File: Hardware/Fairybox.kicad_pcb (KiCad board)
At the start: 2 copper layers, 91.4 x 55.9 mm, 70 parts, among them J1 REED, Q1 locked, Q10 locked, Q2 locked, Q3 locked, Q4 locked, Q5 locked, Q6 locked, Q7 locked, Q8 locked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

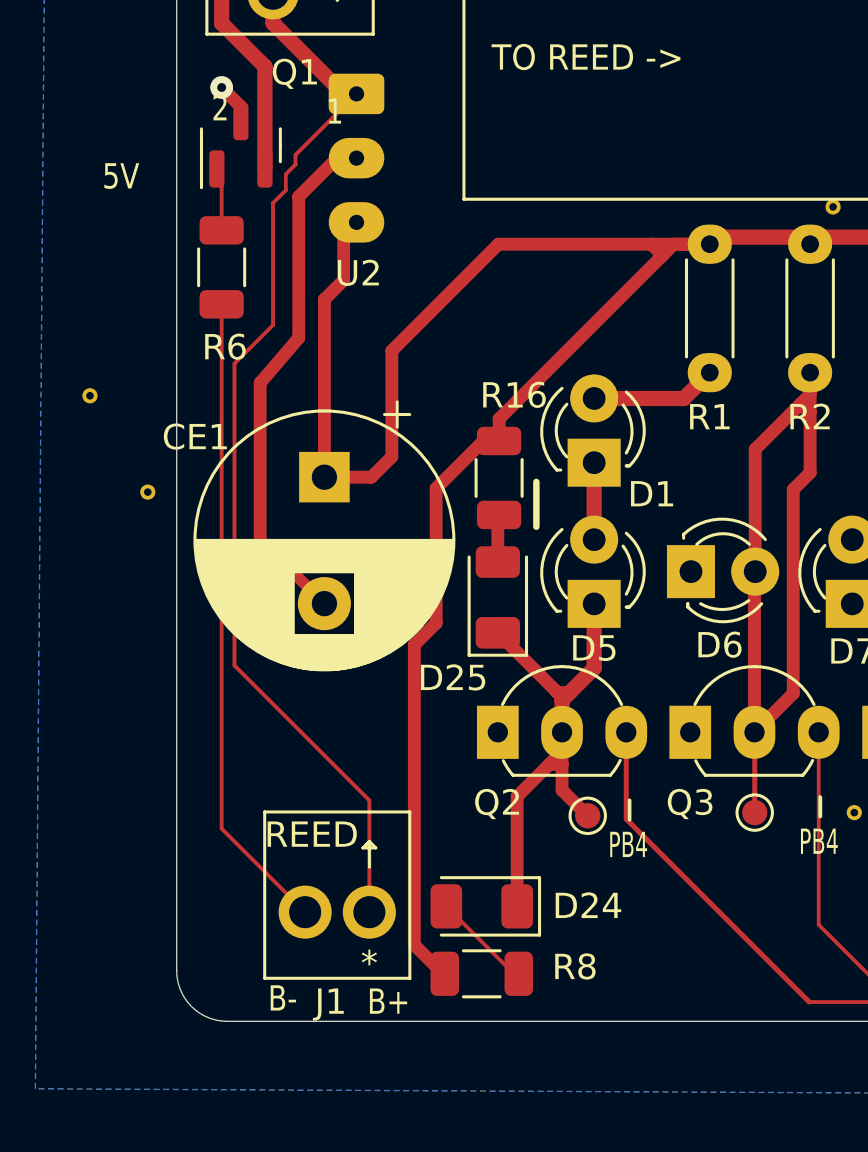
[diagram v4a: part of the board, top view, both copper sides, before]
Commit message: PCB layout tweaks
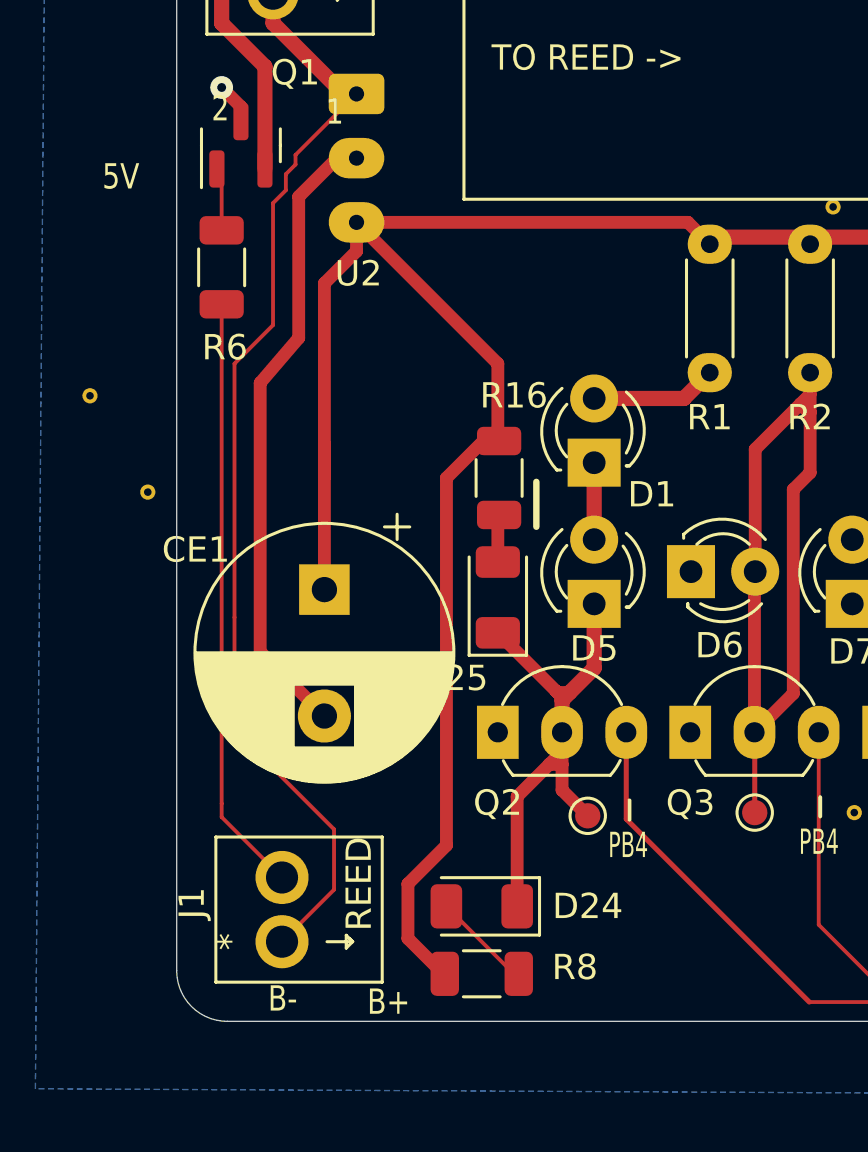
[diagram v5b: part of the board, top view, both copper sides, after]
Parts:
- moved CE1 4.44 mm to (56.6, 89.6)
- moved J1 3.31 mm to (55.7, 103.5), turned to 90 degrees
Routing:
- net GND: track 21.5 -> 26.0 mm
- net +5V: track 156.3 -> 153.6 mm
- net /REED_RETURN: track 25.4 -> 23.7 mm
- net /CHARGE BOARD OUT B+: track 41.3 -> 42.8 mm

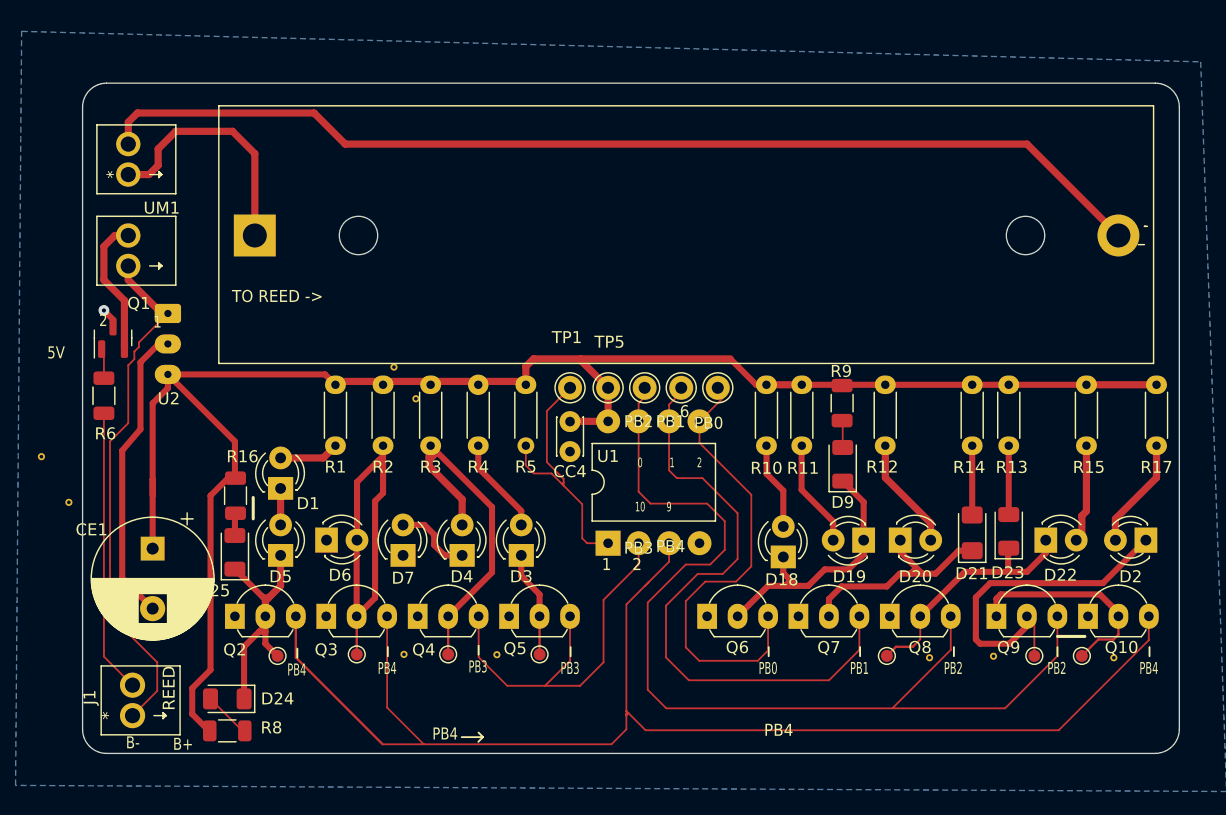
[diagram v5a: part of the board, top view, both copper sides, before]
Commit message: added attiny84 footprint
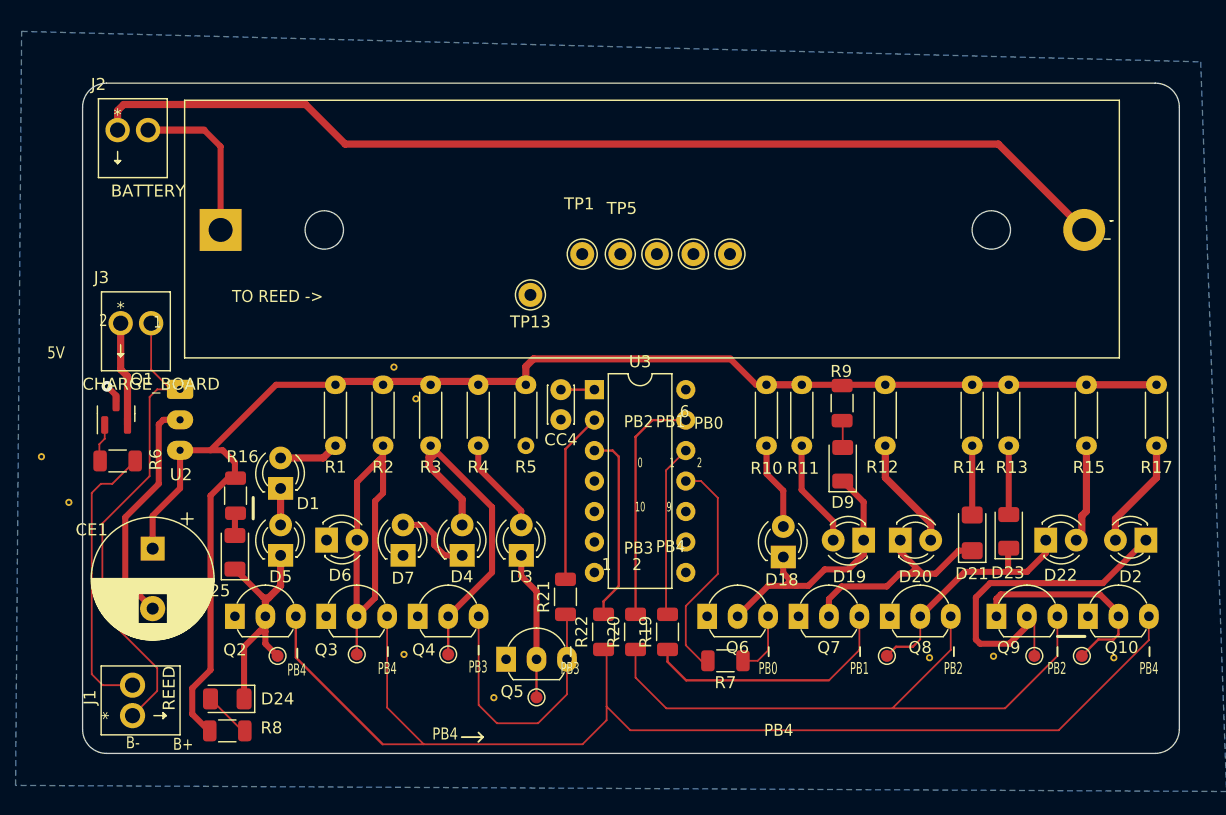
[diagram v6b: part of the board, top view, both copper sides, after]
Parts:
- removed U1: locked, Package_DIP:DIP-8_W10.16mm
- removed UM1: HW-107, UltraLibrary:HW-107 2.54mm terminals
- added J2: BATTERY, UltraLibrary:KF128-2P, F.Cu at (53.7, 55.5)
- added J3: CHARGE_BOARD, UltraLibrary:KF128-2P, F.Cu at (54.0, 71.6)
- added R19: 250R, Resistor_SMD:R_1206_3216Metric, F.Cu at (99.6, 96.5)
- added R20: 250R, Resistor_SMD:R_1206_3216Metric, F.Cu at (96.9, 96.5)
- added R21: 250R, Resistor_SMD:R_1206_3216Metric, F.Cu at (91.1, 93.6)
- added R22: 250R, Resistor_SMD:R_1206_3216Metric, F.Cu at (94.2, 96.5)
- added R7: 250R, Resistor_SMD:R_1206_3216Metric, F.Cu at (104.4, 99.0)
- added TP13: VCC, Connector_Pin:Pin_D1.0mm_L10.0mm, F.Cu at (88.1, 68.5)
- added U3: ATtiny84A-P, Package_DIP:DIP-14_W7.62mm, F.Cu at (93.5, 76.4)
- R8: value ??R -> 470R
- moved TP1 11.2 mm to (92.5, 65.0)
- moved TP2 11.2 mm to (98.7, 65.0)
- moved TP3 11.2 mm to (101.7, 65.0)
- moved TP4 11.2 mm to (104.8, 65.0)
- moved TP5 11.2 mm to (95.6, 65.0)
- moved U2 6.41 mm to (58.9, 76.3)
- moved Q1 6.33 mm to (53.6, 78.4)
- moved R6 5.55 mm to (53.7, 82.3), turned to 180 degrees
- moved Q5 3.59 mm to (86.1, 98.8)
- moved TP9 3.59 mm to (88.6, 102.0)
- moved JP6 3.59 mm to (85.1, 102.0)
- moved BAT1 2.89 mm to (62.3, 62.3)
- moved CC4 2.77 mm to (90.7, 76.4)
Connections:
- CC4 pad 1: +5V -> /CC4_AN
- TP5 pad 1: +5V -> /R18_AN
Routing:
- net /MCU GPIO0 MOSI: track 37.6 -> 5.30 mm
- net /MCU GPIO2 SCK: track 83.4 -> 53.0 mm
- net /MCU GPIO1 MISO: track 50.9 -> 21.3 mm
- net +5V: track 153.6 -> 130.7 mm
- net /MCU RST: track 22.8 -> 0.00 mm
- net /PA0: track 0.00 -> 19.6 mm
- net /PA11: track 0.00 -> 19.0 mm
- net /PB1: track 0.00 -> 15.9 mm
- net /PB0: track 0.00 -> 14.3 mm
- net /PA12: track 0.00 -> 14.2 mm
- net /MCU GPIO4: track 113.5 -> 102.1 mm
- net /MCU GPIO3: track 33.6 -> 23.1 mm
- net /LI-ION_POS: track 20.4 -> 13.6 mm
- net GND: track 26.0 -> 21.1 mm
- net /CHARGE BOARD OUT B+: track 42.8 -> 39.2 mm
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
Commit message: I forget
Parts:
- added D10: BLUE, Diode_SMD:D_1206_3216Metric, F.Cu at (53.3, 63.1)
- added D11: RED, Diode_SMD:D_1206_3216Metric, F.Cu at (56.6, 63.1)
- added Q11: SI2302, Package_TO_SOT_SMD:SOT-23, F.Cu at (112.1, 64.6)
- added Q12: SI2302, Package_TO_SOT_SMD:SOT-23, F.Cu at (112.1, 68.5)
- added R18: 470R, Resistor_SMD:R_1206_3216Metric, F.Cu at (85.7, 77.5)
- added R23: 470R, Resistor_SMD:R_1206_3216Metric, F.Cu at (83.7, 74.2)
- moved JP2 12.5 mm to (70.1, 108.5)
- moved JP1 7.41 mm to (76.2, 70.1)
- moved TP9 6.89 mm to (81.8, 101.3)
- moved Q5 5.46 mm to (83.9, 93.8), turned to -90 degrees
- moved TP6 4.90 mm to (77.1, 101.0)
- moved TP7 3.44 mm to (70.2, 98.7)
- moved R4 2.51 mm to (81.3, 76.1)
- moved Q3 2.39 mm to (72.8, 93.6), turned to -90 degrees
- moved Q4 1.60 mm to (78.3, 93.7), turned to -90 degrees
- moved R3 1.34 mm to (78.5, 76.1)
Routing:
- net Net-(D10-Pad2): track 0.00 -> 26.3 mm
- net Net-(D11-Pad2): track 0.00 -> 13.4 mm
- net /D6_AN: track 33.1 -> 25.4 mm
- net /MCU GPIO3: track 23.1 -> 30.0 mm
- net /Q5_COL: track 12.4 -> 9.06 mm
- net /MCU GPIO4: track 102.1 -> 100.6 mm
- net /Q4_COL: track 29.4 -> 30.4 mm
